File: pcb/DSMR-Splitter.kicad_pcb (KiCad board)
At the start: 2 copper layers, 61.5 x 40.4 mm, 43 parts, among them J1 IN, J2 OUT-A, J3 OUT-B, J4 OUT-C, J5 JTAG, J6 UART, U1 74AHCT1G04, U2 74AHC1G126, U3 74AHCT1G04, U4 74AHCT1G04, U5 74AHCT1G04, U6 TPS76933, U7 EFM32PG12B500, Y1 Crystal_GND24

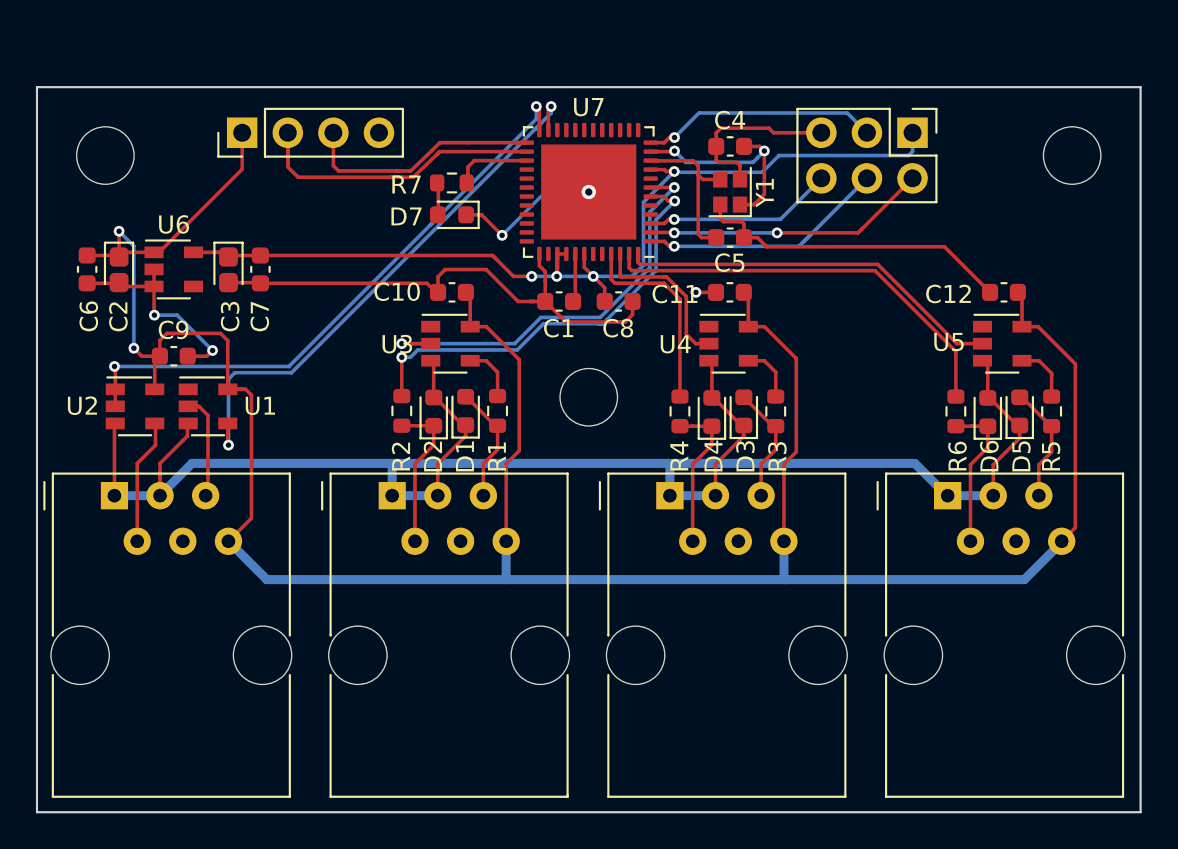
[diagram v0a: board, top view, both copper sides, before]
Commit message: Add board version 2.0.0
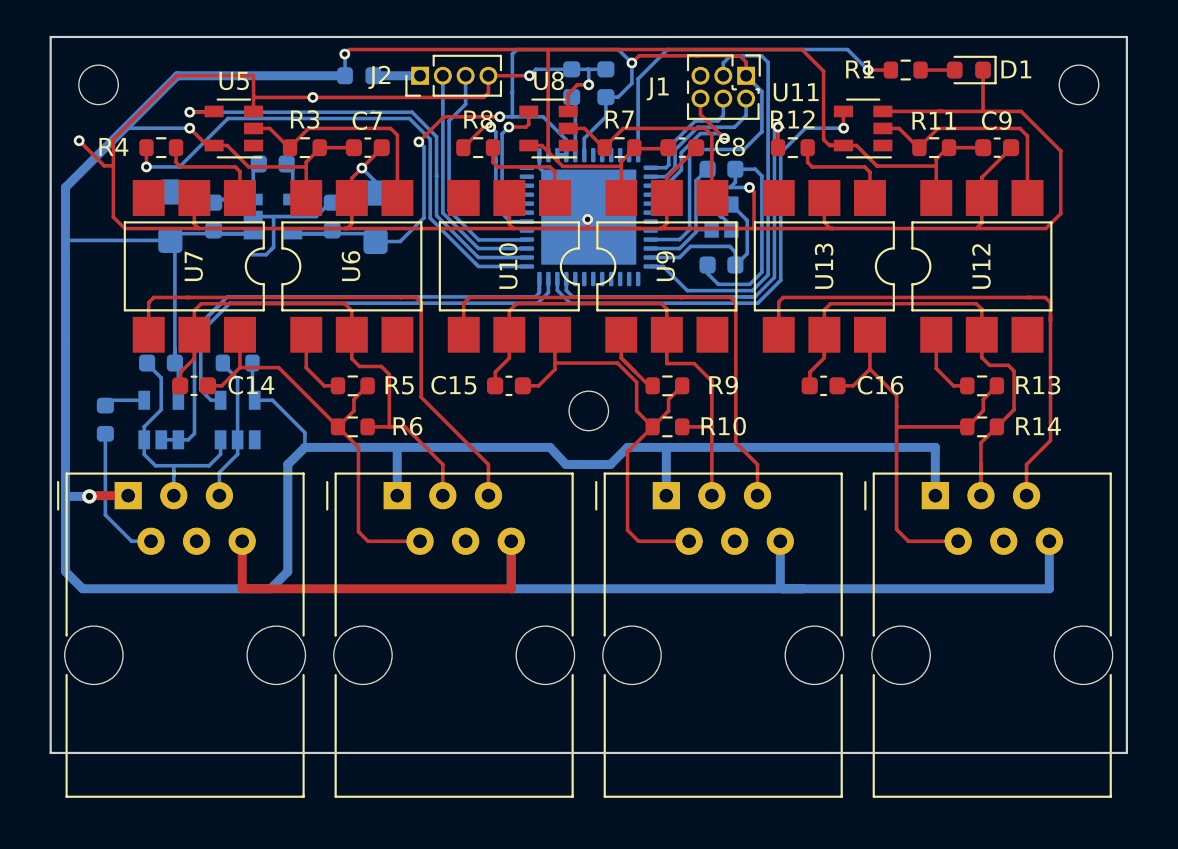
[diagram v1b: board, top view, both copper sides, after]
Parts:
- removed D4, D5, D6: D_TVS, Diode_SMD:D_0603_1608Metric
- removed D7: LED, LED_SMD:LED_0603_1608Metric
- added C13: 1µF, Capacitor_SMD:C_0603_1608Metric, B.Cu at (161.9, 67.6)
- added C14: 100nF, Capacitor_SMD:C_0603_1608Metric, F.Cu at (140.8, 84.5)
- added C15: 100nF, Capacitor_SMD:C_0603_1608Metric, F.Cu at (158.4, 84.5)
- added C16: 100nF, Capacitor_SMD:C_0603_1608Metric, F.Cu at (175.9, 84.5)
- added R10: 100k, Resistor_SMD:R_0603_1608Metric, F.Cu at (167.2, 86.7)
- added R11: 1k, Resistor_SMD:R_0603_1608Metric, F.Cu at (182.1, 71.2)
- added R12: 1k, Resistor_SMD:R_0603_1608Metric, F.Cu at (174.2, 71.2)
- added R13: 2k2, Resistor_SMD:R_0603_1608Metric, F.Cu at (184.7, 84.5)
- added R14: 100k, Resistor_SMD:R_0603_1608Metric, F.Cu at (184.7, 86.7)
- added R8: 1k, Resistor_SMD:R_0603_1608Metric, F.Cu at (156.7, 71.2)
- added R9: 2k2, Resistor_SMD:R_0603_1608Metric, F.Cu at (167.2, 84.5)
- added U10: VOH1016AG-V, Package_DIP:SMDIP-6_W7.62mm, F.Cu at (158.4, 77.8)
- added U11: 74AHCT1G04, Package_TO_SOT_SMD:SOT-23-5, F.Cu at (178.1, 70.1)
- added U12: VOH1016AG-V, Package_DIP:SMDIP-6_W7.62mm, F.Cu at (184.7, 77.8)
- added U13: VOH1016AG-V, Package_DIP:SMDIP-6_W7.62mm, F.Cu at (175.9, 77.8)
- added U8: 74AHCT1G04, Package_TO_SOT_SMD:SOT-23-5, F.Cu at (160.6, 70.1)
- added U9: VOH1016AG-V, Package_DIP:SMDIP-6_W7.62mm, F.Cu at (167.2, 77.8)
- C1: value 1µF -> 100nF; moved to B.Cu
- C10, C6, U4: moved to B.Cu
- C11, C12: value 100nF -> 20pF; moved to B.Cu
- C2: footprint Capacitor_Tantalum_SMD:CP_EIA-1608-08_AVX-J -> Capacitor_Tantalum_SMD:CP_EIA-3216-12_Kemet-S; moved to B.Cu
- C3: value CP -> 100nF; footprint Capacitor_Tantalum_SMD:CP_EIA-1608-08_AVX-J -> Capacitor_SMD:C_0603_1608Metric; moved to B.Cu
- C4: value 20pF -> CP; footprint Capacitor_SMD:C_0603_1608Metric -> Capacitor_Tantalum_SMD:CP_EIA-3216-12_Kemet-S; moved to B.Cu
- C5: value 20pF -> 100nF; moved to B.Cu
- D1: value D_TVS -> LED; footprint Diode_SMD:D_0603_1608Metric -> LED_SMD:LED_0603_1608Metric
- D2, D3: value D_TVS -> 1N4148; moved to B.Cu
- H1, H2, H3: footprint MountingHole:MountingHole_3.2mm_M3 -> MountingHole:MountingHole_2.2mm_M2
- J1: value IN -> JTAG; footprint Connector_RJ:RJ12_Amphenol_54601 -> Connector_PinHeader_1.27mm:PinHeader_2x03_P1.27mm_Vertical
- J2: value OUT-A -> UART; footprint Connector_RJ:RJ12_Amphenol_54601 -> Connector_PinHeader_1.27mm:PinHeader_1x04_P1.27mm_Vertical
- J3: value OUT-B -> IN
- J4: value OUT-C -> OUT-A
- J5: value JTAG -> OUT-B; footprint Connector_PinHeader_2.54mm:PinHeader_2x03_P2.54mm_Vertical -> Connector_RJ:RJ12_Amphenol_54601
- J6: value UART -> OUT-C; footprint Connector_PinHeader_2.54mm:PinHeader_1x04_P2.54mm_Vertical -> Connector_RJ:RJ12_Amphenol_54601
- R2: value 100 -> 1k; moved to B.Cu
- R3, R4, R7: value 100 -> 1k
- R5: value 100 -> 2k2
- R6: value 100 -> 100k
- U1: value 74AHCT1G04 -> EFM32PG12B500; footprint Package_TO_SOT_SMD:SOT-23-5 -> Package_DFN_QFN:QFN-48-1EP_7x7mm_P0.5mm_EP5.3x5.3mm; moved to B.Cu
- U2: value 74AHC1G126 -> TPS76933; moved to B.Cu
- U3: value 74AHCT1G04 -> 74AHC1G126; moved to B.Cu
- U6: value TPS76933 -> VOH1016AG-V; footprint Package_TO_SOT_SMD:SOT-23-5 -> Package_DIP:SMDIP-6_W7.62mm
- U7: value EFM32PG12B500 -> VOH1016AG-V; footprint Package_DFN_QFN:QFN-48-1EP_7x7mm_P0.5mm_EP5.3x5.3mm -> Package_DIP:SMDIP-6_W7.62mm
- Y1: value Crystal_GND24 -> 40MHz; moved to B.Cu
- moved C9 47.3 mm to (185.6, 71.2)
- moved U5 44.4 mm to (143.0, 70.1), turned to 180 degrees
- moved J6 43.6 mm to (182.1, 90.6), turned to 0 degrees
- moved J1 42.2 mm to (171.6, 67.2), turned to 270 degrees
- moved R5 39.0 mm to (149.7, 84.5), turned to 180 degrees
- moved D3 35.6 mm to (135.9, 86.3)
- moved D1 33.9 mm to (184.0, 66.9), turned to 180 degrees
- moved R6 33.6 mm to (149.7, 86.7), turned to 180 degrees
- moved R4 32.4 mm to (139.0, 71.2), turned to 180 degrees
- moved J4 30.7 mm to (152.1, 90.6)
- moved J3 30.2 mm to (137.2, 90.6)
- moved R3 30.1 mm to (147.0, 71.2), turned to 0 degrees
- moved R1 29.6 mm to (180.5, 66.9), turned to 0 degrees
- moved U4 27.7 mm to (143.3, 86.4), turned to 90 degrees
- moved J5 24.4 mm to (167.1, 90.6), turned to 0 degrees
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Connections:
- C1 pad 1: GND -> +5V
- C1 pad 2: Net-(C1-Pad2) -> GND
- C10 pad 1: +5V -> +3V3
- C11 pad 1: +5V -> GND
- C11 pad 2: GND -> Net-(C11-Pad2)
- C12 pad 1: +5V -> GND
- C12 pad 2: GND -> Net-(C12-Pad2)
- C3 pad 1: +3V3 -> Net-(C3-Pad1)
- C4 pad 1: GND -> +3V3
- C4 pad 2: Net-(C4-Pad2) -> GND
- C5 pad 1: GND -> +3V3
- C5 pad 2: Net-(C5-Pad2) -> GND
- C7 pad 1: +3V3 -> +5V
- C8 pad 1: +3V3 -> +5V
- D2 pad 1: Net-(D2-Pad1) -> +5V
- D2 pad 2: GND -> Net-(D2-Pad2)
- D3 pad 1: GND -> Net-(D3-Pad1)
- J1 pad 1: GND -> +3V3
- J1 pad 2: Net-(J1-Pad2) -> /SWDIO
- J1 pad 3: GND -> /RESET
- J1 pad 4: (no net) -> /SWCLK
- J1 pad 5: Net-(J1-Pad5) -> GND
- J1 pad 6: +5V -> /SWO
- J2 pad 1: GND -> Net-(D2-Pad2)
- J2 pad 2: Net-(D2-Pad1) -> /TX
- J2 pad 3: GND -> /RX
- J2 pad 4: (no net) -> GND
- J3 pad 1: GND -> +5V
- J3 pad 2: Net-(D4-Pad1) -> Net-(D3-Pad1)
- J3 pad 5: Net-(D3-Pad2) -> Net-(J3-Pad5)
- J3 pad 6: +5V -> GND
- J4 pad 1: GND -> +5V
- J4 pad 2: Net-(D6-Pad1) -> Net-(C14-Pad2)
- J4 pad 3: GND -> Net-(C14-Pad1)
- J4 pad 5: Net-(D5-Pad2) -> Net-(J4-Pad5)
- J4 pad 6: +5V -> GND
- J5 pad 1: +3V3 -> +5V
- J5 pad 2: /SWDIO -> Net-(C15-Pad2)
- J5 pad 3: /RESET -> Net-(C15-Pad1)
- J5 pad 4: /SWCLK -> (no net)
- J5 pad 5: GND -> Net-(J5-Pad5)
- J5 pad 6: /SWO -> GND
- J6 pad 2: /RX -> Net-(C16-Pad2)
- J6 pad 3: /TX -> Net-(C16-Pad1)
- J6 pad 4: GND -> (no net)
- R1 pad 1: Net-(D1-Pad2) -> /LED
- R1 pad 2: Net-(R1-Pad2) -> Net-(D1-Pad2)
- R2 pad 1: Net-(D2-Pad1) -> +5V
- R2 pad 2: /RTS-A -> Net-(J3-Pad5)
- R3 pad 1: Net-(D3-Pad2) -> Net-(R3-Pad1)
- R3 pad 2: Net-(R3-Pad2) -> +5V
- R4 pad 1: Net-(D4-Pad1) -> Net-(R4-Pad1)
- R4 pad 2: /RTS-B -> /DATA-A
- R5 pad 1: Net-(D5-Pad2) -> Net-(C14-Pad2)
- R6 pad 1: Net-(D6-Pad1) -> Net-(C14-Pad1)
- R6 pad 2: /RTS-C -> Net-(C14-Pad2)
- R7 pad 2: Net-(D7-Pad2) -> +5V
- U1 pad 1: (no net) -> /SWCLK
- U1 pad 2: Net-(J1-Pad5) -> /SWDIO
- U1 pad 3: GND -> /SWO
- U1 pad 4: /DATA -> (no net)
- U1 pad 5: +5V -> (no net)
- U2 pad 1: /RTS -> +5V
- U2 pad 2: /RTS -> GND
- U2 pad 4: Net-(J1-Pad2) -> Net-(C3-Pad1)
- U2 pad 5: +5V -> +3V3
- U3 pad 1: (no net) -> /RTS
- U3 pad 2: /DATA-A -> /RTS
- U3 pad 4: Net-(R1-Pad2) -> Net-(D3-Pad2)
- U4 pad 2: /DATA-B -> Net-(J3-Pad5)
- U4 pad 4: Net-(R3-Pad2) -> /DATA
- U5 pad 2: /DATA-C -> Net-(R3-Pad1)
- U5 pad 4: Net-(R5-Pad2) -> /RTS-A
- U6 pad 1: +5V -> Net-(R5-Pad2)
- U6 pad 2: GND -> Net-(C14-Pad1)
- U6 pad 3: GND -> (no net)
- U6 pad 4: (no net) -> Net-(R3-Pad1)
- U6 pad 5: +3V3 -> GND
- U7 pad 1: /SWCLK -> Net-(R4-Pad1)
- U7 pad 2: /SWDIO -> GND
- U7 pad 3: /SWO -> (no net)
- U7 pad 4: (no net) -> Net-(J4-Pad5)
- U7 pad 5: (no net) -> Net-(C14-Pad1)
- U7 pad 6: /RTS-A -> Net-(C14-Pad2)
- Y1 pad 1: Net-(C4-Pad2) -> Net-(C11-Pad2)
- Y1 pad 3: Net-(C5-Pad2) -> Net-(C12-Pad2)
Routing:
- net GND: track 174.7 -> 254.9 mm, vias 5 -> 7
- net +5V: track 144.3 -> 214.4 mm, vias 2 -> 3
- net Net-(J4-Pad5): track 0.00 -> 30.5 mm
- net Net-(C16-Pad1): track 0.00 -> 29.2 mm
- net Net-(J6-Pad5): track 0.00 -> 29.0 mm
- net Net-(J5-Pad5): track 0.00 -> 28.5 mm
- net Net-(C14-Pad1): track 0.00 -> 28.4 mm
- net Net-(C15-Pad1): track 0.00 -> 27.5 mm
- net Net-(C15-Pad2): track 0.00 -> 25.1 mm
- net Net-(C16-Pad2): track 0.00 -> 24.3 mm
- net Net-(C14-Pad2): track 0.00 -> 23.8 mm
- net /LED: track 0.00 -> 19.5 mm, vias 0 -> 1
- net Net-(R11-Pad1): track 0.00 -> 12.6 mm
- net Net-(R3-Pad1): track 0.00 -> 12.6 mm
- net Net-(C4-Pad2): track 12.5 -> 0.00 mm, vias 2 -> 0
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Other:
- board size 61.5 x 40.4 mm -> 59.9 x 39.9 mm
- board text added: "BasilFX 03/2022 V2.0.0"
- board text removed: "BasilFX 09/2021 V1.0.0"

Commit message: Upgrade project to KiCad 6.0
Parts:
- C2, C4: value CP -> C_Polarized
- U2: value TPS76933 -> TPS76901
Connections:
- net Net-(C14-Pad1) renamed /GND-A
- net Net-(C14-Pad2) renamed /VCC-A
- net Net-(C15-Pad1) renamed /GND-B
- net Net-(C15-Pad2) renamed /VCC-B
- net Net-(C16-Pad1) renamed /GND-C
- net Net-(C16-Pad2) renamed /VCC-C
- J3 pad 4: (no net) -> unconnected-(J3-Pad4)
- J4 pad 4: (no net) -> unconnected-(J4-Pad4)
- J5 pad 4: (no net) -> unconnected-(J5-Pad4)
- J6 pad 4: (no net) -> unconnected-(J6-Pad4)
- U1 pad 13: (no net) -> unconnected-(U1-Pad13)
- U1 pad 14: (no net) -> unconnected-(U1-Pad14)
- U1 pad 15: (no net) -> unconnected-(U1-Pad15)
- U1 pad 16: (no net) -> unconnected-(U1-Pad16)
- U1 pad 17: (no net) -> unconnected-(U1-Pad17)
- U1 pad 18: (no net) -> unconnected-(U1-Pad18)
- U1 pad 19: (no net) -> unconnected-(U1-Pad19)
- U1 pad 20: (no net) -> unconnected-(U1-Pad20)
- U1 pad 29: (no net) -> unconnected-(U1-Pad29)
- U1 pad 32: (no net) -> unconnected-(U1-Pad32)
- U1 pad 33: (no net) -> unconnected-(U1-Pad33)
- U1 pad 34: (no net) -> unconnected-(U1-Pad34)
- U1 pad 35: (no net) -> unconnected-(U1-Pad35)
- U1 pad 36: (no net) -> unconnected-(U1-Pad36)
- U1 pad 38: (no net) -> unconnected-(U1-Pad38)
- U1 pad 4: (no net) -> unconnected-(U1-Pad4)
- U1 pad 43: (no net) -> unconnected-(U1-Pad43)
- U1 pad 44: (no net) -> unconnected-(U1-Pad44)
- U1 pad 45: (no net) -> unconnected-(U1-Pad45)
- U1 pad 46: (no net) -> unconnected-(U1-Pad46)
- U1 pad 47: (no net) -> unconnected-(U1-Pad47)
- U1 pad 5: (no net) -> unconnected-(U1-Pad5)
- U1 pad 6: (no net) -> unconnected-(U1-Pad6)
- U1 pad 7: (no net) -> unconnected-(U1-Pad7)
- U1 pad 8: (no net) -> unconnected-(U1-Pad8)
- U10 pad 3: (no net) -> unconnected-(U10-Pad3)
- U12 pad 3: (no net) -> unconnected-(U12-Pad3)
- U13 pad 3: (no net) -> unconnected-(U13-Pad3)
- U6 pad 3: (no net) -> unconnected-(U6-Pad3)
- U7 pad 3: (no net) -> unconnected-(U7-Pad3)
- U9 pad 3: (no net) -> unconnected-(U9-Pad3)
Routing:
- net GND: track 254.9 -> 245.0 mm
- net +5V: track 214.4 -> 222.4 mm
- net /GND-C: track 29.2 -> 26.1 mm
- net /RTS: track 31.0 -> 28.6 mm
- net Net-(R9-Pad2): track 4.80 -> 3.49 mm
- net +3V3: track 65.2 -> 63.9 mm
- net Net-(J4-Pad5): track 30.5 -> 29.5 mm
- net /DATA-C: track 23.1 -> 22.4 mm
- net Net-(J6-Pad5): track 29.0 -> 28.5 mm
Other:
- net class Default removed
- net class Power removed
- board text added: "BasilFX 10/2022 V2.1.0"
- board text removed: "BasilFX 03/2022 V2.0.0"
